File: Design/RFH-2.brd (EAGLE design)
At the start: 73.3 x 80 mm, 37 parts

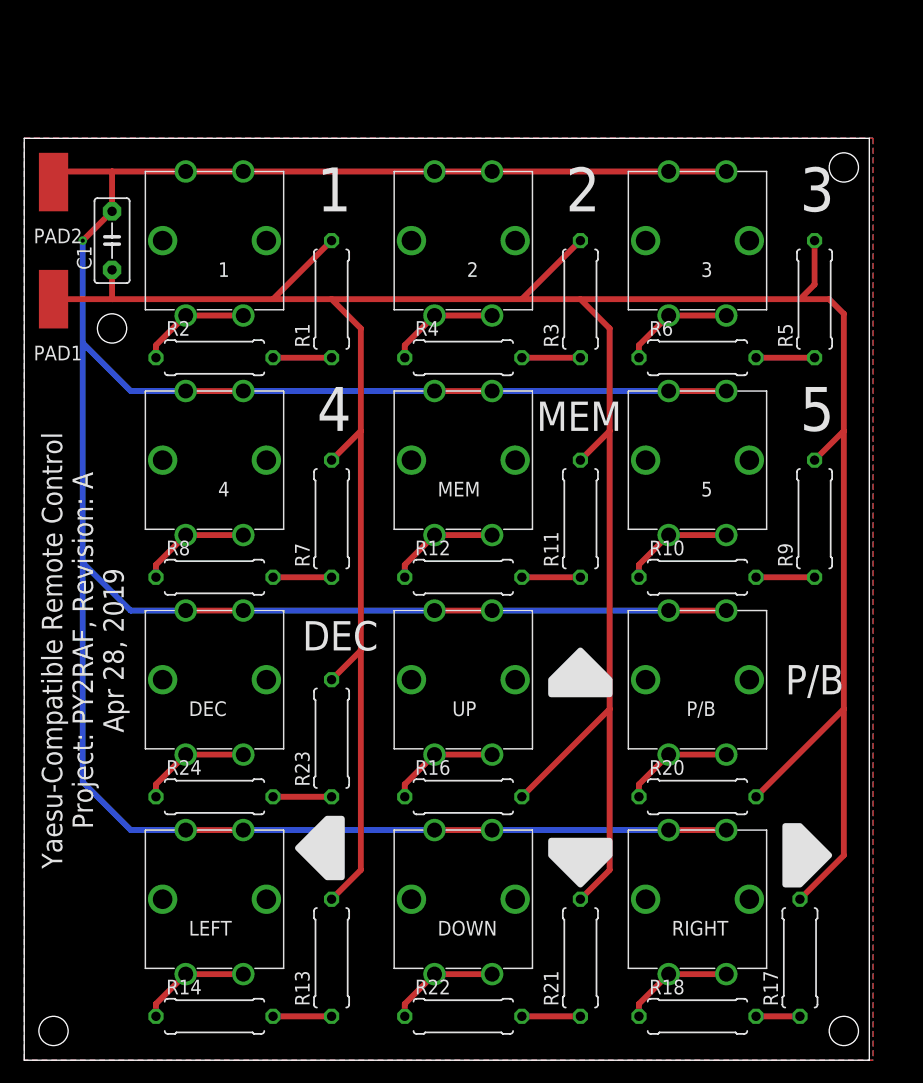
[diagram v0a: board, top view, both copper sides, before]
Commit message: Revision B
* Fixed the push-button pinout
* Now makes extensive use of ground plane
* Rewired the board
* Larger holes, suitable for a screw, with symmetrical holes at the
* board edges
* A through-the-hole pad for the signal input
* Added a few centimeters more to accomodate the $ABOVE changes
* And that's it folks!
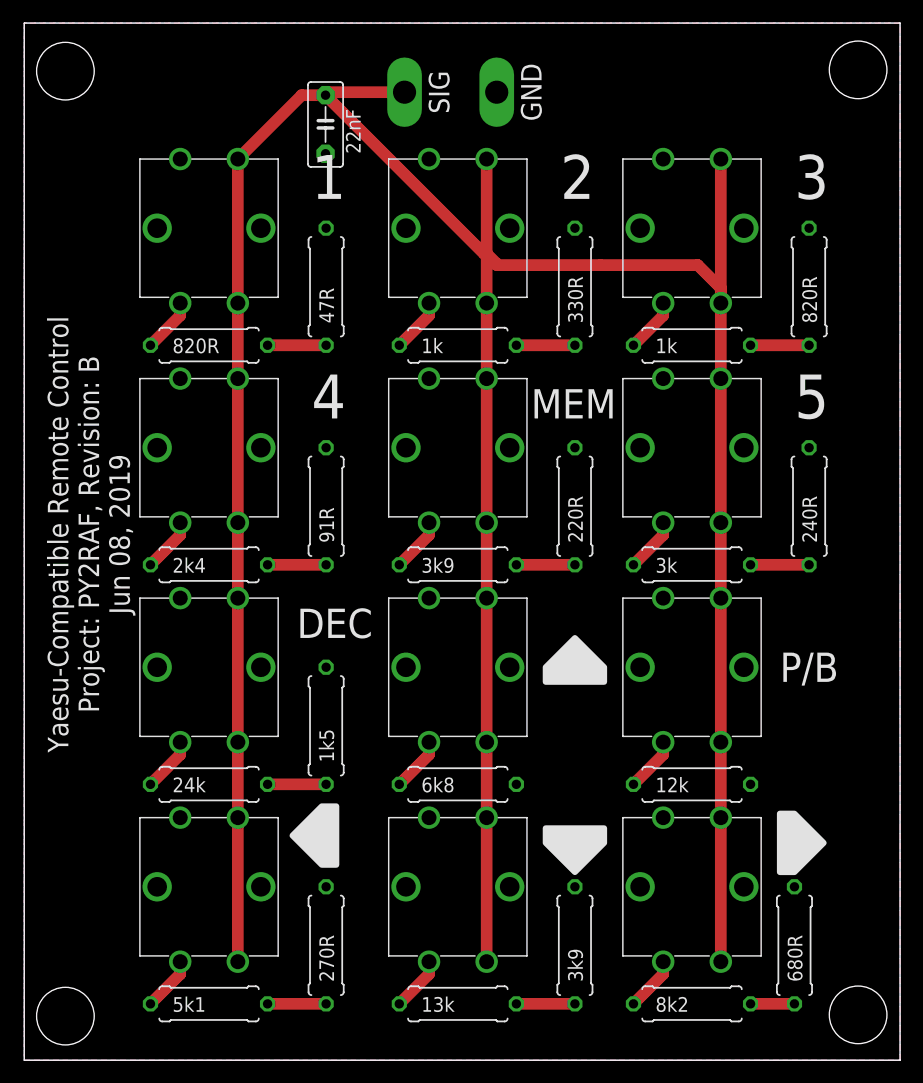
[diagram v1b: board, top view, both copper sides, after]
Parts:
- removed PAD1, PAD2: (no value), wirepad:SMD2,54-5,08
- added TP1, TP2: TPPAD1-20Y, testpad:P1-20Y
- moved C1 21.1 mm to (26.1, 81.2)
- moved R10 1.18 mm to (57.9, 43.0)
- moved R12 1.18 mm to (37.6, 43.0)
- moved R8 1.18 mm to (16.0, 43.0)
- moved R17 1.18 mm to (66.8, 9.97)
- moved R16 1.18 mm to (37.6, 23.9)
- moved R20 1.18 mm to (57.9, 23.9)
- moved R24 1.18 mm to (16.0, 23.9)
- moved DOWN 1.18 mm to (37.6, 15.1)
- moved LEFT 1.18 mm to (16.0, 15.1)
- moved R13 1.18 mm to (26.2, 9.97)
- moved R21 1.18 mm to (47.8, 9.97)
- moved RIGHT 1.18 mm to (57.9, 15.1)
- moved R14 1.18 mm to (16.0, 4.89)
- moved R18 1.18 mm to (57.9, 4.89)
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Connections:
- removed net N$2: C1.1, PAD1.1, R1.2, R11.2, R13.2, R16.2, R17.2, R20.2, R21.2, R23.2, R3.2, R5.2, R7.2, R9.2
- new net GNDA: C1.1, R1.2, R11.2, R13.2, R16.2, R17.2, R20.2, R21.2, R23.2, R3.2, R5.2, R7.2, R9.2, TP1.TP
- net N$1: now also 1.P$6, 2.P$6, 3.P$6, 4.P$6, 5.P$6, DEC.P$6, DOWN.P$6, LEFT.P$6, MEM.P$6, P/B.P$6, RIGHT.P$6, TP2.TP, UP.P$6; no longer 1.P$4, 2.P$4, 3.P$4, 4.P$4, 5.P$4, DEC.P$4, DOWN.P$4, LEFT.P$4, MEM.P$4, P/B.P$4, PAD2.1, RIGHT.P$4, UP.P$4
- net N$10: no longer 2.P$6
- net N$11: no longer 3.P$6
- net N$12: no longer 4.P$6
- net N$13: no longer 5.P$6
- net N$14: no longer MEM.P$6
- net N$3: no longer LEFT.P$6
- net N$4: no longer UP.P$6
- net N$5: no longer RIGHT.P$6
- net N$6: no longer P/B.P$6
- net N$7: no longer DOWN.P$6
- net N$8: no longer 1.P$6
- net N$9: no longer DEC.P$6
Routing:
- net N$2: track 288.3 -> 0.00 mm
- net N$1: track 285.5 -> 268.4 mm, vias 1 -> 0
- net N$12: track 9.73 -> 4.73 mm
- net N$14: track 9.73 -> 4.73 mm
- net N$13: track 9.73 -> 4.73 mm
- net N$9: track 9.73 -> 4.73 mm
- net N$8: track 9.73 -> 4.73 mm
- net N$3: track 9.73 -> 4.73 mm
- net N$11: track 9.73 -> 4.73 mm
- net N$10: track 9.73 -> 4.73 mm
- net N$7: track 9.73 -> 4.73 mm
- net N$6: track 9.73 -> 4.73 mm
- net N$5: track 9.73 -> 4.73 mm
- net N$4: track 9.73 -> 4.73 mm
- added copper zone on layer 1, net GNDA
- added copper zone on layer 16, net GNDA
- removed copper zone on layer 1, net GND
- removed copper zone on layer 16, net GND
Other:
- board size 73.3 x 80 mm -> 76 x 90 mm
- board text added: "GND"
- board text added: "SIG"
- board text added: "Yaesu-Compatible Remote Control Project: PY2RAF, Revision: B Jun 08, 2019"
- board text removed: "Yaesu-Compatible Remote Control Project: PY2RAF, Revision: A Apr 28, 2019"

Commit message: Schematic: Fixes #1
https://github.com/jgedmond pointed a flipped Down Arrow and F/B
button. Thanks for reporting it!
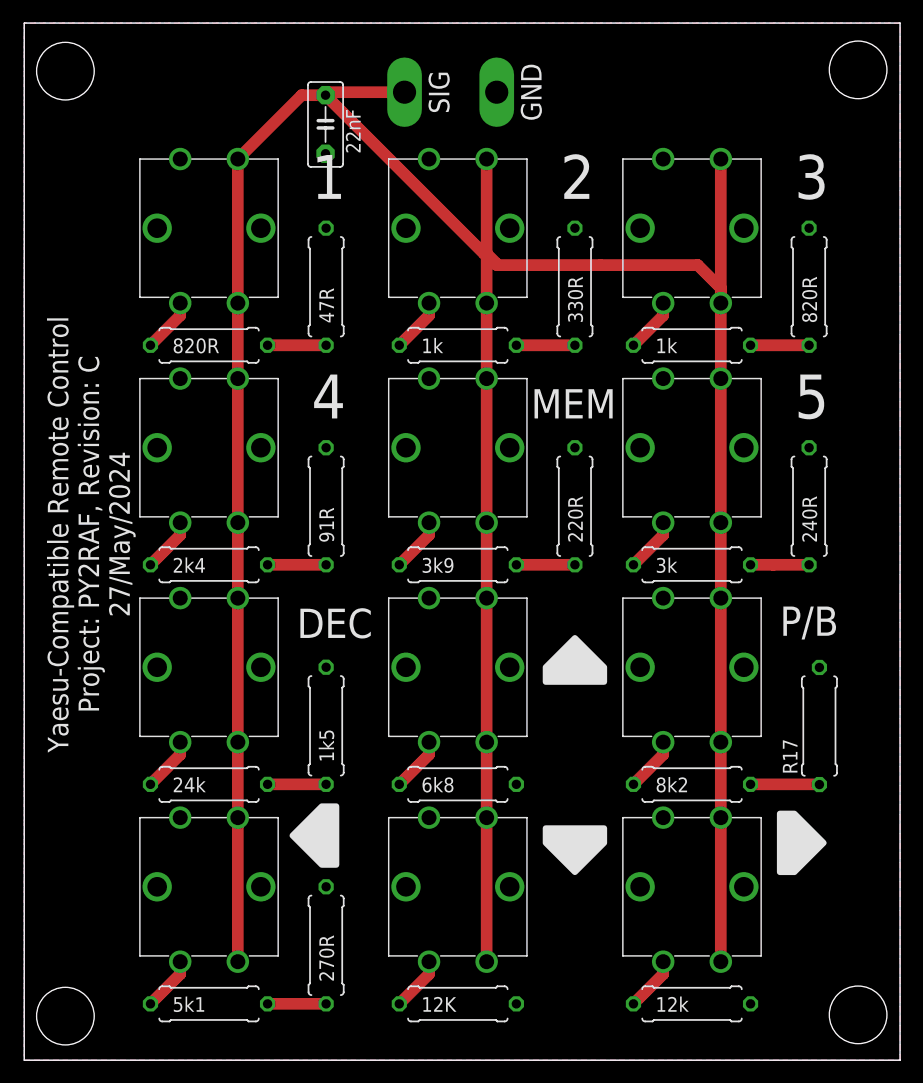
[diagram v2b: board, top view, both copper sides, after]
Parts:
- removed R23: 1k5, rcl:0309/10
- removed R24: 24k, rcl:0309/10
- added R15: 6k8, rcl:0309/10
- R16: value 6k8 -> 12k
- R19: value 13k -> 12K
- R20: value 12k -> 1k5
- R21: value 3k9 -> 24k
- moved R21 34.7 mm to (16.0, 23.9), turned to 0 degrees
- moved R20 32.2 mm to (26.2, 29.0), turned to 90 degrees
- moved R16 27.9 mm to (57.9, 4.89)
- moved R17 19.2 mm to (69.0, 29.0)
- moved R18 19.1 mm to (57.9, 23.9)
- renumbered R22 to R19
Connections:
- removed net N$19: R19.2, R21.1
- net GNDA: now also R15.2, R19.2; no longer R21.2, R23.2
- net N$26: now also R20.1, R21.2; no longer R23.1, R24.2
- net N$4: now also R15.1; no longer R16.1
- net N$5: now also R16.1; no longer R18.1
- net N$6: now also R18.1; no longer R20.1
- net N$9: now also R21.1; no longer R24.1
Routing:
- net N$19: track 5.08 -> 0.00 mm
- net N$2: track 3.81 -> 5.98 mm
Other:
- board text added: "Yaesu-Compatible Remote Control Project: PY2RAF, Revision: C 27/May/2024"
- board text removed: "Yaesu-Compatible Remote Control Project: PY2RAF, Revision: B Jun 08, 2019"
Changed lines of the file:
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@@
 <drawing>
 <settings>
-<setting alwaysvectorfont="yes"/>
+<setting alwaysvectorfont="no"/>
 <setting verticaltext="up"/>
 </settings>
@@
 </polygon>
 <text x="23.655" y="36.64" size="2.54" layer="21" font="vector" ratio="15">DEC</text>
-<text x="65.565" y="32.83" size="2.54" layer="21" font="vector" ratio="15">P/B</text>
+<text x="65.565" y="36.83" size="2.54" layer="21" font="vector" ratio="15">P/B</text>
 <text x="5.605" y="45.64" size="1.778" layer="21" font="vector" rot="R90" align="center">Yaesu-Compatible Remote Control
-Project: PY2RAF, Revision: B
-Jun 08, 2019</text>
+Project: PY2RAF, Revision: C
+27/May/2024</text>
 <text x="26.195" y="50.61" size="1.778" layer="22" font="vector" rot="MR180">VAI CORINTHIANS!</text>
 <hole x="3.572" y="3.826" drill="5"/>
@@
 <attribute name="VALUE" x="12.86" y="4.2042" size="1.27" layer="25" ratio="10"/>
 </element>
-<element name="R16" library="rcl" library_urn="urn:adsk.eagle:library:334" package="0309/10" package3d_urn="urn:adsk.eagle:package:23567/1" value="6k8" x="37.625" y="23.94" smashed="yes">
+<element name="R15" library="rcl" library_urn="urn:adsk.eagle:library:334" package="0309/10" package3d_urn="urn:adsk.eagle:package:23567/1" value="6k8" x="37.625" y="23.94" smashed="yes">
 <attribute name="SPICEPREFIX" value="R" x="56.675" y="-57.34" size="1.778" layer="27" display="off"/>
 <attribute name="VALUE" x="34.45" y="23.2542" size="1.27" layer="25" ratio="10"/>
 </element>
-<element name="R17" library="rcl" library_urn="urn:adsk.eagle:library:334" package="0309/10" package3d_urn="urn:adsk.eagle:package:23567/1" value="680R" x="66.835" y="9.97" smashed="yes" rot="R90">
-<attribute name="SPICEPREFIX" value="R" x="148.115" y="41.72" size="1.778" layer="27" rot="R90" display="off"/>
-<attribute name="VALUE" x="67.5208" y="6.795" size="1.27" layer="25" ratio="10" rot="R90"/>
-</element>
-<element name="R18" library="rcl" library_urn="urn:adsk.eagle:library:334" package="0309/10" package3d_urn="urn:adsk.eagle:package:23567/1" value="8k2" x="57.945" y="4.89" smashed="yes">
+<element name="R16" library="rcl" library_urn="urn:adsk.eagle:library:334" package="0309/10" package3d_urn="urn:adsk.eagle:package:23567/1" value="12k" x="57.945" y="4.89" smashed="yes">
 <attribute name="SPICEPREFIX" value="R" x="102.395" y="-76.39" size="1.778" layer="27" display="off"/>
 <attribute name="VALUE" x="54.77" y="4.2042" size="1.27" layer="25" ratio="10"/>
@@
 <attribute name="VALUE" x="12.86" y="61.3542" size="1.27" layer="25" ratio="10"/>
 </element>
-<element name="R20" library="rcl" library_urn="urn:adsk.eagle:library:334" package="0309/10" package3d_urn="urn:adsk.eagle:package:23567/1" value="12k" x="57.945" y="23.94" smashed="yes">
+<element name="R18" library="rcl" library_urn="urn:adsk.eagle:library:334" package="0309/10" package3d_urn="urn:adsk.eagle:package:23567/1" value="8k2" x="57.945" y="23.94" smashed="yes">
 <attribute name="SPICEPREFIX" value="R" x="115.095" y="-57.34" size="1.778" layer="27" display="off"/>
 <attribute name="VALUE" x="54.77" y="23.2542" size="1.27" layer="25" ratio="10"/>
 </element>
-<element name="R21" library="rcl" library_urn="urn:adsk.eagle:library:334" package="0309/10" package3d_urn="urn:adsk.eagle:package:23567/1" value="3k9" x="47.785" y="9.97" smashed="yes" rot="R90">
-<attribute name="SPICEPREFIX" value="R" x="129.065" y="79.82" size="1.778" layer="27" rot="R90" display="off"/>
-<attribute name="VALUE" x="48.4708" y="6.795" size="1.27" layer="25" ratio="10" rot="R90"/>
-</element>
-<element name="R22" library="rcl" library_urn="urn:adsk.eagle:library:334" package="0309/10" package3d_urn="urn:adsk.eagle:package:23567/1" value="13k" x="37.625" y="4.89" smashed="yes">
+<element name="R19" library="rcl" library_urn="urn:adsk.eagle:library:334" package="0309/10" package3d_urn="urn:adsk.eagle:package:23567/1" value="12K" x="37.625" y="4.89" smashed="yes">
 <attribute name="SPICEPREFIX" value="R" x="56.675" y="-82.74" size="1.778" layer="27" display="off"/>
 <attribute name="VALUE" x="34.45" y="4.2042" size="1.27" layer="25" ratio="10"/>
 </element>
-<element name="R23" library="rcl" library_urn="urn:adsk.eagle:library:334" package="0309/10" package3d_urn="urn:adsk.eagle:package:23567/1" value="1k5" x="26.195" y="29.02" smashed="yes" rot="R90">
+<element name="R20" library="rcl" library_urn="urn:adsk.eagle:library:334" package="0309/10" package3d_urn="urn:adsk.eagle:package:23567/1" value="1k5" x="26.195" y="29.02" smashed="yes" rot="R90">
 <attribute name="SPICEPREFIX" value="R" x="113.825" y="60.77" size="1.778" layer="27" rot="R90" display="off"/>
 <attribute name="VALUE" x="26.8808" y="25.845" size="1.27" layer="25" ratio="10" rot="R90"/>
 </element>
-<element name="R24" library="rcl" library_urn="urn:adsk.eagle:library:334" package="0309/10" package3d_urn="urn:adsk.eagle:package:23567/1" value="24k" x="16.035" y="23.94" smashed="yes">
+<element name="R21" library="rcl" library_urn="urn:adsk.eagle:library:334" package="0309/10" package3d_urn="urn:adsk.eagle:package:23567/1" value="24k" x="16.035" y="23.94" smashed="yes">
 <attribute name="SPICEPREFIX" value="R" x="60.485" y="-63.69" size="1.778" layer="27" display="off"/>
 <attribute name="VALUE" x="12.86" y="23.2542" size="1.27" layer="25" ratio="10"/>
@@
 <element name="TP2" library="testpad" library_urn="urn:adsk.eagle:library:385" package="P1-20Y" package3d_urn="urn:adsk.eagle:package:27951/1" value="TPPAD1-20Y" x="33" y="84" smashed="yes">
 <attribute name="TP_SIGNAL_NAME" value="" x="33" y="84" size="1.778" layer="27" display="off"/>
+</element>
+<element name="R17" library="rcl" library_urn="urn:adsk.eagle:library:334" package="0309/10" package3d_urn="urn:adsk.eagle:package:23567/1" value="680R" x="69" y="29" smashed="yes" rot="R90">
+<attribute name="NAME" x="67.095" y="24.809" size="1.27" layer="25" ratio="10" rot="R90"/>
+<attribute name="SPICEPREFIX" value="R" x="69" y="29" size="1.778" layer="27" rot="R90" display="off"/>
+<attribute name="VALUE" x="69.6858" y="25.825" size="1.27" layer="27" ratio="10" rot="R90"/>
 </element>
 </elements>
@@
 <contactref element="R10" pad="2"/>
 <contactref element="R9" pad="1"/>
-<wire x1="63.025" y1="42.99" x2="68.105" y2="42.99" width="1.016" layer="1"/>
+<wire x1="63.025" y1="42.99" x2="65" y2="42.99" width="1.016" layer="1"/>
+<wire x1="65" y1="42.99" x2="68.105" y2="42.99" width="1.016" layer="1"/>
 </signal>
 <signal name="N$25">
@@
 <signal name="N$4">
 <contactref element="UP" pad="P$5"/>
-<contactref element="R16" pad="1"/>
+<contactref element="R15" pad="1"/>
 <wire x1="32.545" y1="23.94" x2="35.125" y2="26.52" width="1.016" layer="1"/>
 <wire x1="35.125" y1="26.52" x2="35.125" y2="27.6" width="1.016" layer="1"/>
@@
 <signal name="N$5">
 <contactref element="RIGHT" pad="P$5"/>
-<contactref element="R18" pad="1"/>
+<contactref element="R16" pad="1"/>
 <wire x1="52.865" y1="4.89" x2="55.445" y2="7.47" width="1.016" layer="1"/>
 <wire x1="55.445" y1="7.47" x2="55.445" y2="8.55" width="1.016" layer="1"/>
@@
 <signal name="N$6">
 <contactref element="P/B" pad="P$5"/>
-<contactref element="R20" pad="1"/>
+<contactref element="R18" pad="1"/>
 <wire x1="52.865" y1="23.94" x2="55.445" y2="26.52" width="1.016" layer="1"/>
 <wire x1="55.445" y1="26.52" x2="55.445" y2="27.6" width="1.016" layer="1"/>
@@
 <signal name="N$7">
 <contactref element="DOWN" pad="P$5"/>
-<contactref element="R22" pad="1"/>
+<contactref element="R19" pad="1"/>
 <wire x1="32.545" y1="4.89" x2="35.125" y2="7.47" width="1.016" layer="1"/>
 <wire x1="35.125" y1="7.47" x2="35.125" y2="8.55" width="1.016" layer="1"/>
@@
 <signal name="N$9">
 <contactref element="DEC" pad="P$5"/>
-<contactref element="R24" pad="1"/>
+<contactref element="R21" pad="1"/>
 <wire x1="10.955" y1="23.94" x2="13.535" y2="26.52" width="1.016" layer="1"/>
 <wire x1="13.535" y1="26.52" x2="13.535" y2="27.6" width="1.016" layer="1"/>
@@
 <wire x1="21.115" y1="4.89" x2="26.195" y2="4.89" width="1.016" layer="1"/>
 </signal>
-<signal name="N$17">
-<contactref element="R18" pad="2"/>
-<contactref element="R17" pad="1"/>
-<wire x1="63.025" y1="4.89" x2="66.835" y2="4.89" width="1.016" layer="1"/>
-</signal>
-<signal name="N$19">
-<contactref element="R22" pad="2"/>
-<contactref element="R21" pad="1"/>
-<wire x1="42.705" y1="4.89" x2="47.785" y2="4.89" width="1.016" layer="1"/>
-</signal>
 <signal name="N$26">
-<contactref element="R24" pad="2"/>
-<contactref element="R23" pad="1"/>
+<contactref element="R21" pad="2"/>
+<contactref element="R20" pad="1"/>
 <wire x1="21.115" y1="23.94" x2="26.195" y2="23.94" width="1.016" layer="1"/>
 </signal>
@@
 <vertex x="76" y="90"/>
 </polygon>
-<contactref element="R23" pad="2"/>
+<contactref element="R20" pad="2"/>
 <contactref element="R13" pad="2"/>
-<contactref element="R17" pad="2"/>
-<contactref element="R21" pad="2"/>
 <contactref element="R11" pad="2"/>
 <contactref element="R9" pad="2"/>
@@
 <contactref element="R1" pad="2"/>
 <contactref element="C1" pad="1"/>
+<contactref element="R15" pad="2"/>
+<contactref element="TP1" pad="TP"/>
+<contactref element="R17" pad="2"/>
 <contactref element="R16" pad="2"/>
-<contactref element="R20" pad="2"/>
-<contactref element="TP1" pad="TP"/>
+<contactref element="R19" pad="2"/>
 </signal>
 <signal name="N$1">
@@
 <wire x1="50" y1="69" x2="58.445" y2="69" width="1.016" layer="1"/>
 </signal>
+<signal name="N$2">
+<contactref element="R18" pad="2"/>
+<contactref element="R17" pad="1"/>
+<wire x1="63.025" y1="23.94" x2="68.98" y2="23.94" width="1.016" layer="1"/>
+<wire x1="68.98" y1="23.94" x2="69" y2="23.92" width="1.016" layer="1"/>
+</signal>
 </signals>
